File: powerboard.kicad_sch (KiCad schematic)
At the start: 27 parts, among them J1 B03B, J2 EMER_SW, J3 EMER_SW, Q1 TJ60S04M3L, U1 PQQ10W-Q24-S5-S, U2 TLP222A

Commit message: ツェナーで定電圧チャレンジ
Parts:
- removed R3, R4: 10k, Resistor_THT:R_Axial_DIN0207_L6.3mm_D2.5mm_P7.62mm_Horizontal, symbol Device:R
- added D5: BZX55C9V1, Diode_THT:D_DO-35_SOD27_P10.16mm_Horizontal, symbol Diode:ZPDxx
- R2: value 10k -> 1k8
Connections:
- net VDD: now also D5.1 (K); no longer R2.1
- new net: D5.2 (A), R2.1
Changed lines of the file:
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@@
 	(paper "A4")
+	(junction
+		(at 144.78 66.04)
+		(diameter 0)
+		(color 0 0 0 0)
+	)
 	(junction
 		(at 154.94 76.2)
@@
 		(color 0 0 0 0)
 	)
-	(junction
-		(at 144.78 68.58)
-		(diameter 0)
-		(color 0 0 0 0)
-	)
 	(no_connect
 		(at 97.79 33.02)
@@
 	(wire
 		(pts
-			(xy 144.78 62.23) (xy 144.78 68.58)
+			(xy 144.78 57.15) (xy 144.78 66.04)
 		)
 		(stroke
@@
 	(wire
 		(pts
-			(xy 144.78 68.58) (xy 144.78 71.12)
+			(xy 55.88 41.91) (xy 39.37 41.91)
 		)
 		(stroke
@@
 	(wire
 		(pts
-			(xy 55.88 41.91) (xy 39.37 41.91)
+			(xy 67.31 69.85) (xy 80.01 69.85)
 		)
 		(stroke
@@
 	(wire
 		(pts
-			(xy 67.31 69.85) (xy 80.01 69.85)
+			(xy 82.55 69.85) (xy 86.36 69.85)
 		)
 		(stroke
@@
 	(wire
 		(pts
-			(xy 82.55 69.85) (xy 86.36 69.85)
+			(xy 96.52 38.1) (xy 97.79 38.1)
 		)
 		(stroke
@@
 	(wire
 		(pts
-			(xy 96.52 38.1) (xy 97.79 38.1)
+			(xy 97.79 74.93) (xy 97.79 77.47)
 		)
 		(stroke
@@
 	(wire
 		(pts
-			(xy 97.79 74.93) (xy 97.79 77.47)
+			(xy 60.96 39.37) (xy 59.69 39.37)
 		)
 		(stroke
@@
 	(wire
 		(pts
-			(xy 60.96 39.37) (xy 59.69 39.37)
+			(xy 25.4 71.12) (xy 33.02 71.12)
 		)
 		(stroke
@@
 	(wire
 		(pts
-			(xy 25.4 71.12) (xy 33.02 71.12)
+			(xy 55.88 41.91) (xy 55.88 43.18)
 		)
 		(stroke
@@
 	(wire
 		(pts
-			(xy 55.88 41.91) (xy 55.88 43.18)
+			(xy 144.78 83.82) (xy 144.78 81.28)
 		)
 		(stroke
@@
 	(wire
 		(pts
-			(xy 144.78 83.82) (xy 144.78 81.28)
+			(xy 156.21 76.2) (xy 154.94 76.2)
 		)
 		(stroke
@@
 	(wire
 		(pts
-			(xy 156.21 76.2) (xy 154.94 76.2)
+			(xy 96.52 44.45) (xy 96.52 43.18)
 		)
 		(stroke
@@
 	(wire
 		(pts
-			(xy 96.52 44.45) (xy 96.52 43.18)
+			(xy 152.4 66.04) (xy 154.94 66.04)
 		)
 		(stroke
@@
 	(wire
 		(pts
-			(xy 144.78 68.58) (xy 154.94 68.58)
+			(xy 144.78 66.04) (xy 144.78 71.12)
 		)
 		(stroke
@@
 		)
 	)
+	(wire
+		(pts
+			(xy 154.94 66.04) (xy 154.94 68.58)
+		)
+		(stroke
+			(width 0)
+			(type default)
+		)
+	)
 	(global_label "sig"
 		(shape input)
@@
 	)
 	(symbol
-		(lib_id "power:GNDPWR")
-		(at 154.94 91.44 0)
-		(unit 1)
-		(exclude_from_sim no)
-		(in_bom yes)
-		(on_board yes)
-		(dnp no)
-		(fields_autoplaced yes)
-		(property "Reference" "#PWR012"
-			(at 154.94 96.52 0)
-			(effects
-				(font
-					(size 1.27 1.27)
-				)
-				(hide yes)
-			)
-		)
-		(property "Value" "GNDPWR"
-			(at 154.813 95.25 0)
-			(effects
-				(font
-					(size 1.27 1.27)
-				)
-			)
-		)
-		(property "Footprint" ""
-			(at 154.94 92.71 0)
-			(effects
-				(font
-					(size 1.27 1.27)
-				)
-				(hide yes)
-			)
-		)
-		(property "Datasheet" ""
-			(at 154.94 92.71 0)
-			(effects
-				(font
-					(size 1.27 1.27)
-				)
-				(hide yes)
-			)
-		)
-		(property "Description" "Power symbol creates a global label with name \"GNDPWR\" , global ground"
-			(at 154.94 91.44 0)
-			(effects
-				(font
-					(size 1.27 1.27)
-				)
-				(hide yes)
-			)
-		)
-		(pin "1"
-		)
-		(instances
-			(project "powerboard"
-				(path "/f61afb78-be8f-4a5f-ad16-61c0881e4198"
-					(reference "#PWR012")
-					(unit 1)
-				)
-			)
-		)
-	)
-	(symbol
 		(lib_id "Connector:Conn_01x02_Socket")
 		(at 181.61 81.28 180)
@@
 	(symbol
 		(lib_id "power:VDD")
-		(at 144.78 62.23 0)
+		(at 144.78 57.15 0)
 		(unit 1)
 		(exclude_from_sim no)
@@
 		(fields_autoplaced yes)
 		(property "Reference" "#PWR011"
-			(at 144.78 66.04 0)
+			(at 144.78 60.96 0)
 			(effects
 				(font
@@
 		)
 		(property "Value" "VDD"
+			(at 144.78 52.07 0)
+			(effects
+				(font
+					(size 1.27 1.27)
+				)
+			)
+		)
+		(property "Footprint" ""
 			(at 144.78 57.15 0)
 			(effects
@@
 					(size 1.27 1.27)
 				)
-			)
-		)
-		(property "Footprint" ""
-			(at 144.78 62.23 0)
-			(effects
-				(font
-					(size 1.27 1.27)
-				)
 				(hide yes)
 			)
 		)
 		(property "Datasheet" ""
-			(at 144.78 62.23 0)
+			(at 144.78 57.15 0)
 			(effects
 				(font
@@
 		)
 		(property "Description" "Power symbol creates a global label with name \"VDD\""
-			(at 144.78 62.23 0)
+			(at 144.78 57.15 0)
 			(effects
 				(font
@@
 	)
 	(symbol
-		(lib_id "Device:R")
-		(at 154.94 87.63 0)
-		(unit 1)
-		(exclude_from_sim no)
-		(in_bom yes)
-		(on_board yes)
-		(dnp no)
-		(property "Reference" "R4"
-			(at 149.86 86.36 0)
-			(effects
-				(font
-					(size 1.27 1.27)
-				)
-				(justify left)
-			)
-		)
-		(property "Value" "10k"
-			(at 149.86 88.9 0)
-			(effects
-				(font
-					(size 1.27 1.27)
-				)
-				(justify left)
-			)
-		)
-		(property "Footprint" "Resistor_THT:R_Axial_DIN0207_L6.3mm_D2.5mm_P7.62mm_Horizontal"
-			(at 153.162 87.63 90)
-			(effects
-				(font
-					(size 1.27 1.27)
-				)
-				(hide yes)
-			)
-		)
-		(property "Datasheet" "~"
-			(at 154.94 87.63 0)
-			(effects
-				(font
-					(size 1.27 1.27)
-				)
-				(hide yes)
-			)
-		)
-		(property "Description" "Resistor"
-			(at 154.94 87.63 0)
-			(effects
-				(font
-					(size 1.27 1.27)
-				)
-				(hide yes)
-			)
-		)
-		(pin "1"
-		)
-		(pin "2"
-		)
-		(instances
-			(project "powerboard"
-				(path "/f61afb78-be8f-4a5f-ad16-61c0881e4198"
-					(reference "R4")
-					(unit 1)
-				)
-			)
-		)
-	)
-	(symbol
 		(lib_id "power:GNDPWR")
 		(at 96.52 44.45 0)
@@
 	)
 	(symbol
-		(lib_id "Device:R")
-		(at 154.94 80.01 0)
-		(unit 1)
-		(exclude_from_sim no)
-		(in_bom yes)
-		(on_board yes)
-		(dnp no)
-		(property "Reference" "R3"
-			(at 149.86 78.74 0)
-			(effects
-				(font
-					(size 1.27 1.27)
-				)
-				(justify left)
-			)
-		)
-		(property "Value" "10k"
-			(at 149.86 81.28 0)
-			(effects
-				(font
-					(size 1.27 1.27)
-				)
-				(justify left)
-			)
-		)
-		(property "Footprint" "Resistor_THT:R_Axial_DIN0207_L6.3mm_D2.5mm_P7.62mm_Horizontal"
-			(at 153.162 80.01 90)
-			(effects
-				(font
-					(size 1.27 1.27)
-				)
-				(hide yes)
-			)
-		)
-		(property "Datasheet" "~"
-			(at 154.94 80.01 0)
-			(effects
-				(font
-					(size 1.27 1.27)
-				)
-				(hide yes)
-			)
-		)
-		(property "Description" "Resistor"
-			(at 154.94 80.01 0)
-			(effects
-				(font
-					(size 1.27 1.27)
-				)
-				(hide yes)
-			)
-		)
-		(pin "1"
-		)
-		(pin "2"
-		)
-		(instances
-			(project "powerboard"
-				(path "/f61afb78-be8f-4a5f-ad16-61c0881e4198"
-					(reference "R3")
-					(unit 1)
-				)
-			)
-		)
-	)
-	(symbol
 		(lib_id "power:PWR_FLAG")
 		(at 252.73 67.31 180)
@@
 	)
 	(symbol
+		(lib_id "Diode:ZPDxx")
+		(at 148.59 66.04 0)
+		(unit 1)
+		(exclude_from_sim no)
+		(in_bom yes)
+		(on_board yes)
+		(dnp no)
+		(fields_autoplaced yes)
+		(property "Reference" "D5"
+			(at 148.59 59.69 0)
+			(effects
+				(font
+					(size 1.27 1.27)
+				)
+			)
+		)
+		(property "Value" "BZX55C9V1"
+			(at 148.59 62.23 0)
+			(effects
+				(font
+					(size 1.27 1.27)
+				)
+			)
+		)
+		(property "Footprint" "Diode_THT:D_DO-35_SOD27_P10.16mm_Horizontal"
+			(at 148.59 70.485 0)
+			(effects
+				(font
+					(size 1.27 1.27)
+				)
+				(hide yes)
+			)
+		)
+		(property "Datasheet" "http://diotec.com/tl_files/diotec/files/pdf/datasheets/zpd1"
+			(at 148.59 66.04 0)
+			(effects
+				(font
+					(size 1.27 1.27)
+				)
+				(hide yes)
+			)
+		)
+		(property "Description" "500mW Zener Diode, DO-35"
+			(at 148.59 66.04 0)
+			(effects
+				(font
+					(size 1.27 1.27)
+				)
+				(hide yes)
+			)
+		)
+		(pin "2"
+		)
+		(pin "1"
+		)
+		(instances
+			(project ""
+				(path "/f61afb78-be8f-4a5f-ad16-61c0881e4198"
+					(reference "D5")
+					(unit 1)
+				)
+			)
+		)
+	)
+	(symbol
 		(lib_id "Device:R")
 		(at 154.94 72.39 0)
@@
 			)
 		)
-		(property "Value" "10k"
+		(property "Value" "1k8"
 			(at 149.86 72.39 0)
 			(effects

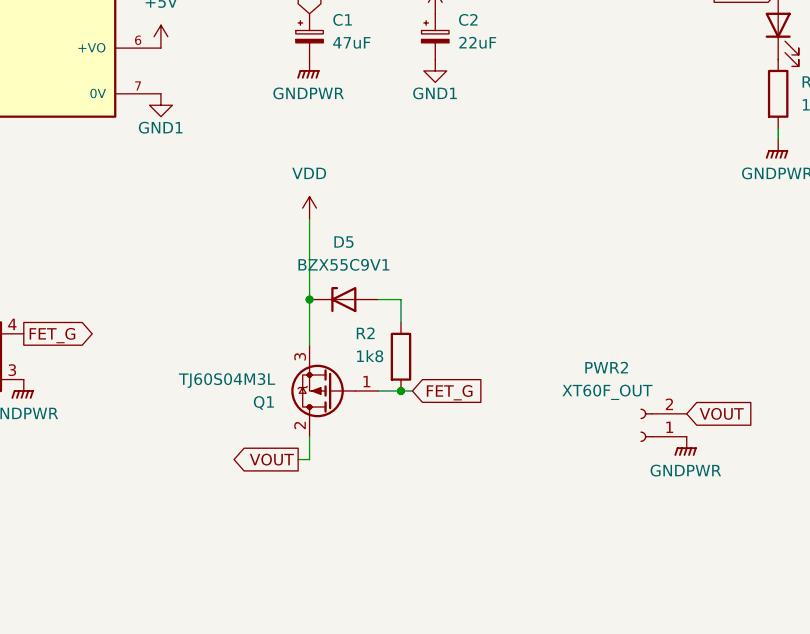
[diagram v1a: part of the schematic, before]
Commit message: ツェナー回り修正、DCDC入力コンデンサ位置変更
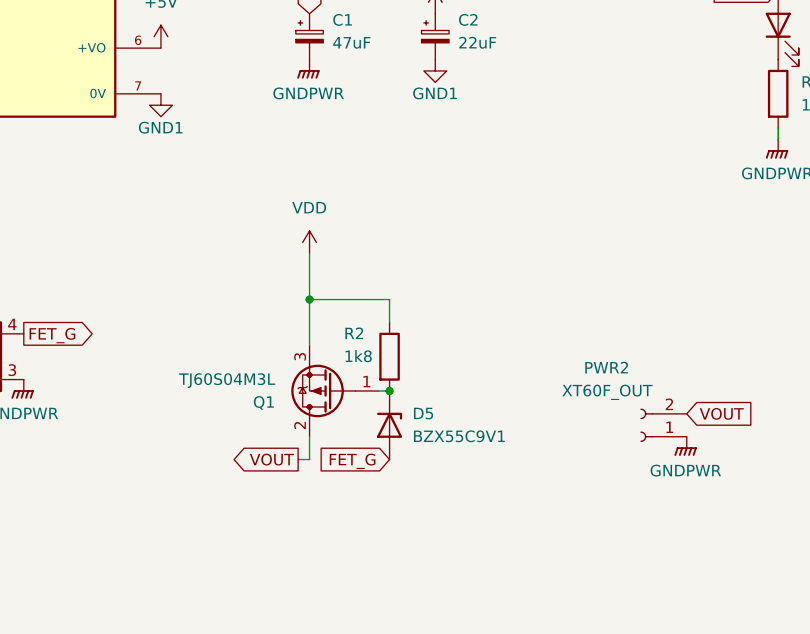
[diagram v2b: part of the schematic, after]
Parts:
- D5: footprint Diode_THT:D_DO-35_SOD27_P10.16mm_Horizontal -> Diode_THT:D_DO-35_SOD27_P7.62mm_Horizontal
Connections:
- net FET_G: now also D5.2 (A); no longer Q1.1 (G), R2.2
- net VDD: now also R2.1; no longer D5.1 (K)
- new net: D5.1 (K), Q1.1 (G), R2.2
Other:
- moved on the sheet: D5, R2
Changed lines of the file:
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@@
 	(paper "A4")
+	(junction
+		(at 153.67 76.2)
+		(diameter 0)
+		(color 0 0 0 0)
+	)
 	(junction
 		(at 144.78 66.04)
@@
 		(color 0 0 0 0)
 	)
-	(junction
-		(at 154.94 76.2)
-		(diameter 0)
-		(color 0 0 0 0)
-	)
 	(no_connect
 		(at 97.79 33.02)
@@
 	(wire
 		(pts
-			(xy 154.94 76.2) (xy 152.4 76.2)
+			(xy 59.69 69.85) (xy 64.77 69.85)
 		)
 		(stroke
@@
 	(wire
 		(pts
-			(xy 59.69 69.85) (xy 64.77 69.85)
+			(xy 96.52 43.18) (xy 97.79 43.18)
 		)
 		(stroke
@@
 	(wire
 		(pts
-			(xy 96.52 43.18) (xy 97.79 43.18)
+			(xy 25.4 73.66) (xy 33.02 73.66)
 		)
 		(stroke
@@
 	(wire
 		(pts
-			(xy 25.4 73.66) (xy 33.02 73.66)
+			(xy 144.78 60.96) (xy 144.78 66.04)
 		)
 		(stroke
@@
 	(wire
 		(pts
-			(xy 144.78 57.15) (xy 144.78 66.04)
+			(xy 44.45 39.37) (xy 39.37 39.37)
 		)
 		(stroke
@@
 	(wire
 		(pts
-			(xy 44.45 39.37) (xy 39.37 39.37)
+			(xy 196.85 48.26) (xy 196.85 46.99)
 		)
 		(stroke
@@
 	(wire
 		(pts
-			(xy 196.85 48.26) (xy 196.85 46.99)
+			(xy 55.88 41.91) (xy 39.37 41.91)
 		)
 		(stroke
@@
 	(wire
 		(pts
-			(xy 55.88 41.91) (xy 39.37 41.91)
+			(xy 67.31 69.85) (xy 80.01 69.85)
 		)
 		(stroke
@@
 	(wire
 		(pts
-			(xy 67.31 69.85) (xy 80.01 69.85)
+			(xy 82.55 69.85) (xy 86.36 69.85)
 		)
 		(stroke
@@
 	(wire
 		(pts
-			(xy 82.55 69.85) (xy 86.36 69.85)
+			(xy 144.78 66.04) (xy 144.78 71.12)
 		)
 		(stroke
@@
 	(wire
 		(pts
-			(xy 97.79 74.93) (xy 97.79 77.47)
+			(xy 153.67 76.2) (xy 152.4 76.2)
 		)
 		(stroke
@@
 	(wire
 		(pts
-			(xy 60.96 39.37) (xy 59.69 39.37)
+			(xy 97.79 74.93) (xy 97.79 77.47)
 		)
 		(stroke
@@
 	(wire
 		(pts
-			(xy 25.4 71.12) (xy 33.02 71.12)
+			(xy 144.78 66.04) (xy 153.67 66.04)
 		)
 		(stroke
@@
 	(wire
 		(pts
-			(xy 55.88 41.91) (xy 55.88 43.18)
+			(xy 60.96 39.37) (xy 59.69 39.37)
 		)
 		(stroke
@@
 	(wire
 		(pts
-			(xy 144.78 83.82) (xy 144.78 81.28)
+			(xy 25.4 71.12) (xy 33.02 71.12)
 		)
 		(stroke
@@
 	(wire
 		(pts
-			(xy 156.21 76.2) (xy 154.94 76.2)
+			(xy 55.88 41.91) (xy 55.88 43.18)
 		)
 		(stroke
@@
 	(wire
 		(pts
-			(xy 96.52 44.45) (xy 96.52 43.18)
+			(xy 144.78 83.82) (xy 144.78 81.28)
 		)
 		(stroke
@@
 	(wire
 		(pts
-			(xy 152.4 66.04) (xy 154.94 66.04)
+			(xy 96.52 44.45) (xy 96.52 43.18)
 		)
 		(stroke
@@
 	(wire
 		(pts
-			(xy 144.78 66.04) (xy 144.78 71.12)
+			(xy 93.98 69.85) (xy 97.79 69.85)
 		)
 		(stroke
@@
 	(wire
 		(pts
-			(xy 93.98 69.85) (xy 97.79 69.85)
+			(xy 153.67 66.04) (xy 153.67 68.58)
 		)
 		(stroke
@@
 		)
 	)
-	(wire
-		(pts
-			(xy 154.94 66.04) (xy 154.94 68.58)
-		)
-		(stroke
-			(width 0)
-			(type default)
-		)
-	)
 	(global_label "sig"
 		(shape input)
@@
 	(global_label "FET_G"
 		(shape input)
-		(at 156.21 76.2 0)
+		(at 153.67 83.82 180)
 		(fields_autoplaced yes)
 		(effects
@@
 				(size 1.27 1.27)
 			)
-			(justify left)
+			(justify right)
 		)
 		(property "Intersheetrefs" "${INTERSHEET_REFS}"
-			(at 164.638 76.2 0)
-			(effects
-				(font
-					(size 1.27 1.27)
-				)
-				(justify left)
+			(at 145.242 83.82 0)
+			(effects
+				(font
+					(size 1.27 1.27)
+				)
+				(justify right)
 				(hide yes)
 			)
@@
 	(symbol
 		(lib_id "power:VDD")
-		(at 144.78 57.15 0)
+		(at 144.78 60.96 0)
 		(unit 1)
 		(exclude_from_sim no)
@@
 		(fields_autoplaced yes)
 		(property "Reference" "#PWR011"
+			(at 144.78 64.77 0)
+			(effects
+				(font
+					(size 1.27 1.27)
+				)
+				(hide yes)
+			)
+		)
+		(property "Value" "VDD"
+			(at 144.78 55.88 0)
+			(effects
+				(font
+					(size 1.27 1.27)
+				)
+			)
+		)
+		(property "Footprint" ""
 			(at 144.78 60.96 0)
 			(effects
@@
 			)
 		)
-		(property "Value" "VDD"
-			(at 144.78 52.07 0)
-			(effects
-				(font
-					(size 1.27 1.27)
-				)
-			)
-		)
-		(property "Footprint" ""
-			(at 144.78 57.15 0)
-			(effects
-				(font
-					(size 1.27 1.27)
-				)
-				(hide yes)
-			)
-		)
 		(property "Datasheet" ""
-			(at 144.78 57.15 0)
+			(at 144.78 60.96 0)
 			(effects
 				(font
@@
 		)
 		(property "Description" "Power symbol creates a global label with name \"VDD\""
-			(at 144.78 57.15 0)
+			(at 144.78 60.96 0)
 			(effects
 				(font
@@
 	(symbol
 		(lib_id "Diode:ZPDxx")
-		(at 148.59 66.04 0)
+		(at 153.67 80.01 270)
 		(unit 1)
 		(exclude_from_sim no)
@@
 		(fields_autoplaced yes)
 		(property "Reference" "D5"
-			(at 148.59 59.69 0)
-			(effects
-				(font
-					(size 1.27 1.27)
-				)
+			(at 156.21 78.7399 90)
+			(effects
+				(font
+					(size 1.27 1.27)
+				)
+				(justify left)
 			)
 		)
 		(property "Value" "BZX55C9V1"
-			(at 148.59 62.23 0)
-			(effects
-				(font
-					(size 1.27 1.27)
-				)
-			)
-		)
-		(property "Footprint" "Diode_THT:D_DO-35_SOD27_P10.16mm_Horizontal"
-			(at 148.59 70.485 0)
+			(at 156.21 81.2799 90)
+			(effects
+				(font
+					(size 1.27 1.27)
+				)
+				(justify left)
+			)
+		)
+		(property "Footprint" "Diode_THT:D_DO-35_SOD27_P7.62mm_Horizontal"
+			(at 149.225 80.01 0)
 			(effects
 				(font
@@
 		)
 		(property "Datasheet" "http://diotec.com/tl_files/diotec/files/pdf/datasheets/zpd1"
-			(at 148.59 66.04 0)
+			(at 153.67 80.01 0)
 			(effects
 				(font
@@
 		)
 		(property "Description" "500mW Zener Diode, DO-35"
-			(at 148.59 66.04 0)
+			(at 153.67 80.01 0)
 			(effects
 				(font
@@
 	(symbol
 		(lib_id "Device:R")
-		(at 154.94 72.39 0)
+		(at 153.67 72.39 0)
 		(unit 1)
 		(exclude_from_sim no)
@@
 		(dnp no)
 		(property "Reference" "R2"
-			(at 149.86 69.85 0)
+			(at 148.59 69.85 0)
 			(effects
 				(font
@@
 		)
 		(property "Value" "1k8"
-			(at 149.86 72.39 0)
+			(at 148.59 72.39 0)
 			(effects
 				(font
@@
 		)
 		(property "Footprint" "Resistor_THT:R_Axial_DIN0207_L6.3mm_D2.5mm_P7.62mm_Horizontal"
-			(at 153.162 72.39 90)
+			(at 151.892 72.39 90)
 			(effects
 				(font
@@
 		)
 		(property "Datasheet" "~"
-			(at 154.94 72.39 0)
+			(at 153.67 72.39 0)
 			(effects
 				(font
@@
 		)
 		(property "Description" ""
-			(at 154.94 72.39 0)
-			(effects
-				(font
+			(at 153.67 72.39 0)
+			(effects
+				(font

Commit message: コンデンサ追加、フップリ修正
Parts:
- added C3: C_Polarized, Capacitor_THT:CP_Radial_D16.0mm_P7.50mm, symbol Device:C_Polarized
- C1: footprint Capacitor_THT:C_Radial_D5.0mm_H11.0mm_P2.00mm -> Capacitor_THT:CP_Radial_D6.3mm_P2.50mm
- C2: footprint Capacitor_THT:C_Radial_D5.0mm_H11.0mm_P2.00mm -> Capacitor_THT:CP_Radial_D5.0mm_P2.00mm
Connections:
- net GNDPWR: now also C3.2
- net VOUT: now also C3.1
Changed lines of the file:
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@@
 	(paper "A4")
 	(junction
+		(at 198.12 83.82)
+		(diameter 0)
+		(color 0 0 0 0)
+	)
+	(junction
 		(at 153.67 76.2)
 		(diameter 0)
@@
 	(wire
 		(pts
+			(xy 198.12 76.2) (xy 186.69 76.2)
+		)
+		(stroke
+			(width 0)
+			(type default)
+		)
+	)
+	(wire
+		(pts
 			(xy 96.52 43.18) (xy 97.79 43.18)
 		)
@@
 	(wire
 		(pts
+			(xy 198.12 83.82) (xy 186.69 83.82)
+		)
+		(stroke
+			(width 0)
+			(type default)
+		)
+	)
+	(wire
+		(pts
 			(xy 25.4 71.12) (xy 33.02 71.12)
 		)
@@
 	(wire
 		(pts
+			(xy 186.69 83.82) (xy 186.69 81.28)
+		)
+		(stroke
+			(width 0)
+			(type default)
+		)
+	)
+	(wire
+		(pts
+			(xy 186.69 76.2) (xy 186.69 78.74)
+		)
+		(stroke
+			(width 0)
+			(type default)
+		)
+	)
+	(wire
+		(pts
 			(xy 93.98 69.85) (xy 97.79 69.85)
 		)
@@
 	(global_label "VOUT"
 		(shape input)
-		(at 186.69 78.74 0)
+		(at 198.12 76.2 90)
 		(fields_autoplaced yes)
 		(effects
@@
 		)
 		(property "Intersheetrefs" "${INTERSHEET_REFS}"
-			(at 195.118 78.74 0)
+			(at 198.12 68.4976 90)
 			(effects
 				(font
@@
 			)
 		)
-		(property "Footprint" "Capacitor_THT:C_Radial_D5.0mm_H11.0mm_P2.00mm"
+		(property "Footprint" "Capacitor_THT:CP_Radial_D6.3mm_P2.50mm"
 			(at 144.78 36.83 0)
 			(effects
@@
 			)
 		)
-		(property "Footprint" "Capacitor_THT:C_Radial_D5.0mm_H11.0mm_P2.00mm"
+		(property "Footprint" "Capacitor_THT:CP_Radial_D5.0mm_P2.00mm"
 			(at 158.75 36.83 0)
 			(effects
@@
 	(symbol
 		(lib_id "power:GNDPWR")
-		(at 186.69 81.28 0)
+		(at 198.12 83.82 0)
 		(unit 1)
 		(exclude_from_sim no)
@@
 		(fields_autoplaced yes)
 		(property "Reference" "#PWR015"
-			(at 186.69 86.36 0)
+			(at 198.12 88.9 0)
 			(effects
 				(font
@@
 		)
 		(property "Value" "GNDPWR"
-			(at 186.563 85.09 0)
+			(at 197.993 87.63 0)
 			(effects
 				(font
@@
 		)
 		(property "Footprint" ""
-			(at 186.69 82.55 0)
+			(at 198.12 85.09 0)
 			(effects
 				(font
@@
 		)
 		(property "Datasheet" ""
-			(at 186.69 82.55 0)
+			(at 198.12 85.09 0)
 			(effects
 				(font
@@
 		)
 		(property "Description" "Power symbol creates a global label with name \"GNDPWR\" , global ground"
-			(at 186.69 81.28 0)
+			(at 198.12 83.82 0)
 			(effects
 				(font
@@
 					(unit 1)
 				)
+			)
+		)
+	)
+	(symbol
+		(lib_id "Device:C_Polarized")
+		(at 198.12 80.01 0)
+		(unit 1)
+		(exclude_from_sim no)
+		(in_bom yes)
+		(on_board yes)
+		(dnp no)
+		(fields_autoplaced yes)
+		(property "Reference" "C3"
+			(at 201.93 77.8509 0)
+			(effects
+				(font
+					(size 1.27 1.27)
+				)
+				(justify left)
+			)
+		)
+		(property "Value" "C_Polarized"
+			(at 201.93 80.3909 0)
+			(effects
+				(font
+					(size 1.27 1.27)
+				)
+				(justify left)
+			)
+		)
+		(property "Footprint" "Capacitor_THT:CP_Radial_D16.0mm_P7.50mm"
+			(at 199.0852 83.82 0)
+			(effects
+				(font
+					(size 1.27 1.27)
+				)
+				(hide yes)
+			)
+		)
+		(property "Datasheet" "~"
+			(at 198.12 80.01 0)
+			(effects
+				(font
+					(size 1.27 1.27)
+				)
+				(hide yes)
+			)
+		)
+		(property "Description" "Polarized capacitor"
+			(at 198.12 80.01 0)
+			(effects
+				(font
+					(size 1.27 1.27)
+				)
+				(hide yes)
+			)
+		)
+		(pin "2"
+		)
+		(pin "1"
+		)
+		(instances
+			(project ""
+				(path "/f61afb78-be8f-4a5f-ad16-61c0881e4198"
+					(reference "C3")
+					(unit 1)
+				)

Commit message: あれこれ
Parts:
- H1, H2, H3, H4: footprint MountingHole:MountingHole_3.2mm_M3 -> MountingHole:MountingHole_3.2mm_M3_Pad_Via
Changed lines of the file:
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@@
 			)
 		)
-		(property "Footprint" "MountingHole:MountingHole_3.2mm_M3"
+		(property "Footprint" "MountingHole:MountingHole_3.2mm_M3_Pad_Via"
 			(at 248.92 95.25 0)
 			(effects
@@
 			)
 		)
-		(property "Footprint" "MountingHole:MountingHole_3.2mm_M3"
+		(property "Footprint" "MountingHole:MountingHole_3.2mm_M3_Pad_Via"
 			(at 248.92 90.17 0)
 			(effects
@@
 			)
 		)
-		(property "Footprint" "MountingHole:MountingHole_3.2mm_M3"
+		(property "Footprint" "MountingHole:MountingHole_3.2mm_M3_Pad_Via"
 			(at 248.92 100.33 0)
 			(effects
@@
 			)
 		)
-		(property "Footprint" "MountingHole:MountingHole_3.2mm_M3"
+		(property "Footprint" "MountingHole:MountingHole_3.2mm_M3_Pad_Via"
 			(at 248.92 85.09 0)
 			(effects
